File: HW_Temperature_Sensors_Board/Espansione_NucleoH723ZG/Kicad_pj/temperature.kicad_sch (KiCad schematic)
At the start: 18 parts, among them IC1 MAX31855TASA+, J1 Screw_Terminal_01x02, J2 NB-PTCO-126, U1 MCP6477

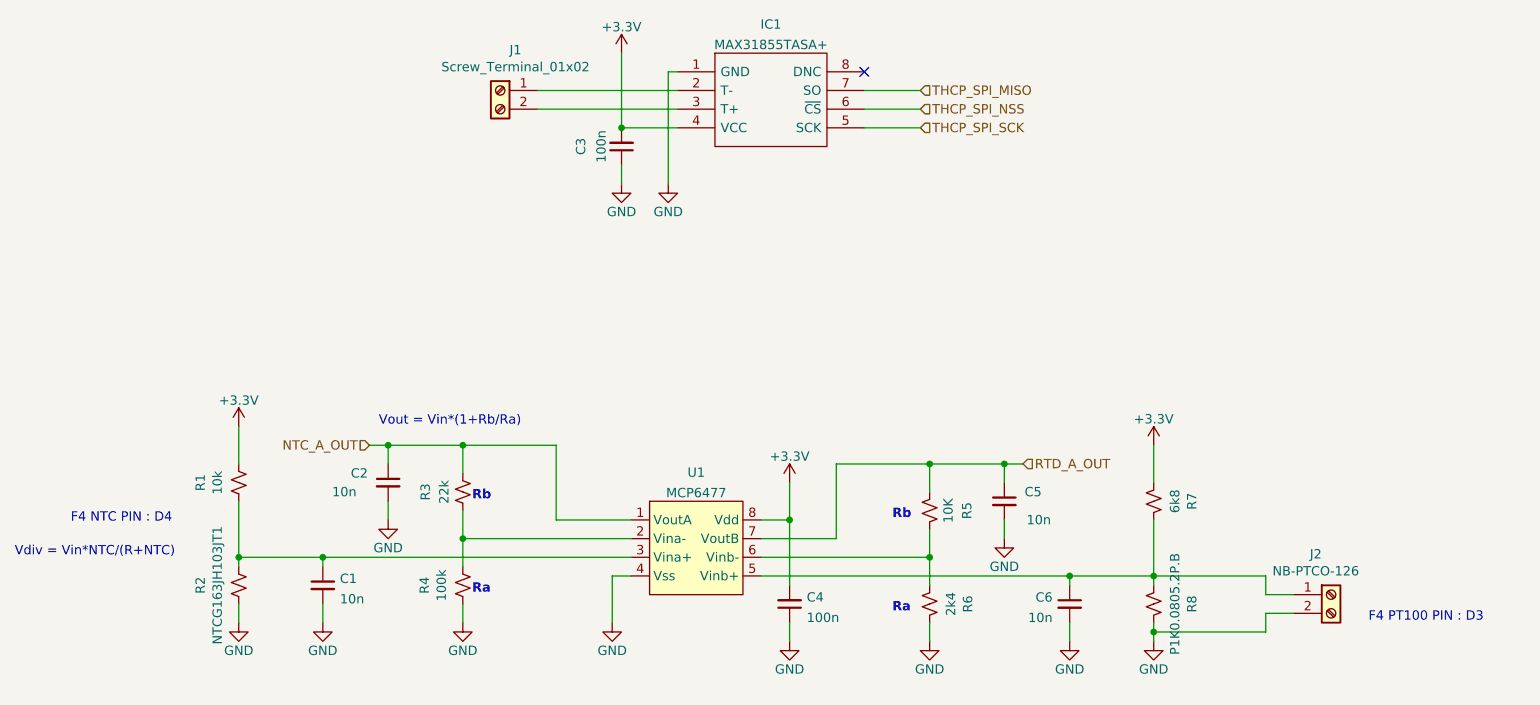
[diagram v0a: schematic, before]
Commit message: doc+fw: update excel and change of C1, C2
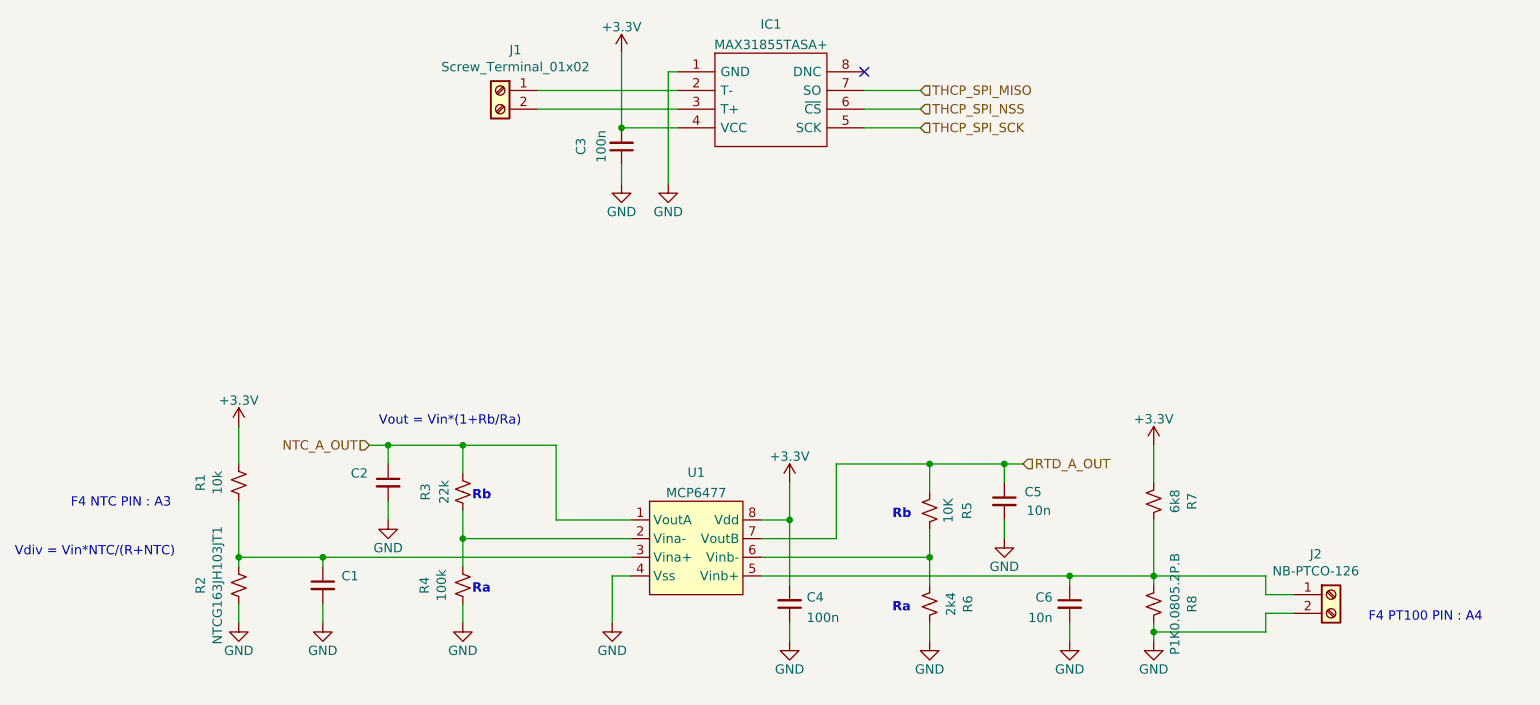
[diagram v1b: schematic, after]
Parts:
- C1, C2: value 10n -> (none)
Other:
- note added: "F4 NTC PIN : A3"
- note added: "F4 PT100 PIN : A4"
- note removed: "F4 NTC PIN : D4"
- note removed: "F4 PT100 PIN : D3"
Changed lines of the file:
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@@
     (effects (font (size 1.27 1.27) (thickness 0.254) bold) (justify left bottom))
   )
-  (text "F4 PT100 PIN : D3" (at 237.49 123.19 0)
+  (text "F4 PT100 PIN : A4\n" (at 237.49 123.19 0)
     (effects (font (size 1.27 1.27)) (justify left bottom))
   )
@@
     (effects (font (size 1.27 1.27)) (justify left bottom))
   )
-  (text "F4 NTC PIN : D4\n\n" (at 60.96 111.76 0)
+  (text "F4 NTC PIN : A3\n\n\n" (at 60.96 111.76 0)
     (effects (font (size 1.27 1.27)) (justify left bottom))
   )
@@
       (effects (font (size 1.27 1.27)) (justify left))
     )
-    (property "Value" "10n" (id 1) (at 194.31 109.22 0)
+    (property "Value" "10n" (id 1) (at 194.31 107.95 0)
       (effects (font (size 1.27 1.27)) (justify left))
     )
@@
       (effects (font (size 1.27 1.27)) (justify left))
     )
-    (property "Value" "10n" (id 1) (at 96.52 105.41 0)
+    (property "Value" "" (id 1) (at 99.06 105.41 0)
       (effects (font (size 1.27 1.27)) (justify left))
     )
@@
   (symbol (lib_id "Device:C_Small") (at 95.25 118.11 0) (unit 1)
     (in_bom yes) (on_board yes) (fields_autoplaced)
-    (property "Reference" "C1" (id 0) (at 97.5741 117.2078 0)
-      (effects (font (size 1.27 1.27)) (justify left))
-    )
-    (property "Value" "10n" (id 1) (at 97.5741 119.9829 0)
-      (effects (font (size 1.27 1.27)) (justify left))
-    )
+    (property "Reference" "C1" (id 0) (at 97.79 116.8462 0)
+      (effects (font (size 1.27 1.27)) (justify left))
+    )
+    (property "Value" "" (id 1) (at 97.79 119.3862 0)
+      (effects (font (size 1.27 1.27)) (justify left))
+    )

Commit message: fix: longer preset time and further calibration
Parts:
- C1, C2: value (none) -> 1u
- R2: value NTCG163JH103JT1 -> NTCG063JH103JT1
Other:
- note removed: "F4 NTC PIN : A3"
- note removed: "F4 PT100 PIN : A4"
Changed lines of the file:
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@@
     (stroke (width 0) (type default) (color 0 0 0 0))
   )
-  (image (at 48.26 135.89) (scale 0.33)
+  (image (at 43.18 173.99) (scale 0.33)
     (data
       iVBORw0KGgoAAAANSUhEUgAABosAAAPhCAYAAAAhK5YdAAAABHNCSVQICAgIfAhkiAAAAAlwSFlz
@@
     )
   )
-  (image (at 247.65 85.09) (scale 0.33)
+  (image (at 245.11 54.61) (scale 0.33)
     (data
       iVBORw0KGgoAAAANSUhEUgAABwEAAAPhCAYAAAARgtAVAAAABHNCSVQICAgIfAhkiAAAAAlwSFlz
@@
     (effects (font (size 1.27 1.27) (thickness 0.254) bold) (justify left bottom))
   )
-  (text "F4 PT100 PIN : A4\n" (at 237.49 123.19 0)
-    (effects (font (size 1.27 1.27)) (justify left bottom))
-  )
-  (text "Vdiv = Vin*NTC/(R+NTC)" (at 53.34 114.3 0)
-    (effects (font (size 1.27 1.27)) (justify left bottom))
-  )
-  (text "F4 NTC PIN : A3\n\n\n" (at 60.96 111.76 0)
+  (text "Vdiv = Vin*NTC/(R+NTC)" (at 82.55 132.08 0)
     (effects (font (size 1.27 1.27)) (justify left bottom))
   )
@@
       (effects (font (size 1.27 1.27)) (justify left))
     )
-    (property "Value" "" (id 1) (at 99.06 105.41 0)
+    (property "Value" "1u" (id 1) (at 99.06 105.41 0)
       (effects (font (size 1.27 1.27)) (justify left))
     )
@@
     (in_bom yes) (on_board yes)
     (property "Reference" "R2" (id 0) (at 78.613 118.11 90))
-    (property "Value" "NTCG163JH103JT1" (id 1) (at 80.9244 118.11 90))
+    (property "Value" "NTCG063JH103JT1" (id 1) (at 80.9244 118.11 90))
     (property "Footprint" "Resistor_SMD:R_0603_1608Metric_Pad0.98x0.95mm_HandSolder" (id 2) (at 83.82 118.11 0)
       (effects (font (size 1.27 1.27)) hide)
@@
       (effects (font (size 1.27 1.27)) (justify left))
     )
-    (property "Value" "" (id 1) (at 97.79 119.3862 0)
+    (property "Value" "1u" (id 1) (at 97.79 119.3862 0)
       (effects (font (size 1.27 1.27)) (justify left))
     )
